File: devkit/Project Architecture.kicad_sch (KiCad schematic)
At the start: 0 parts

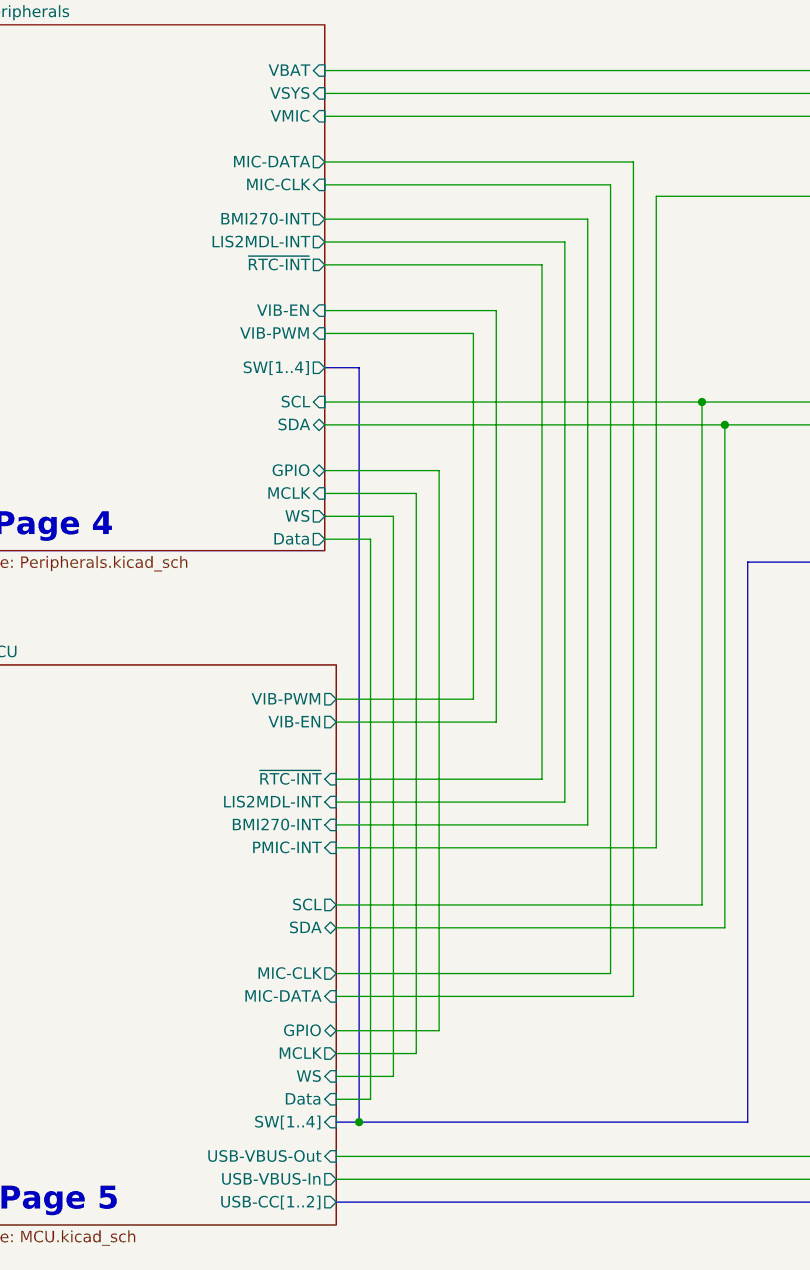
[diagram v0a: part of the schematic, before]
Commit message: Revert "Feature: Issue #180"
This reverts commit 364f4bbc8b17cbfb7f0155205af3315526997ba0.
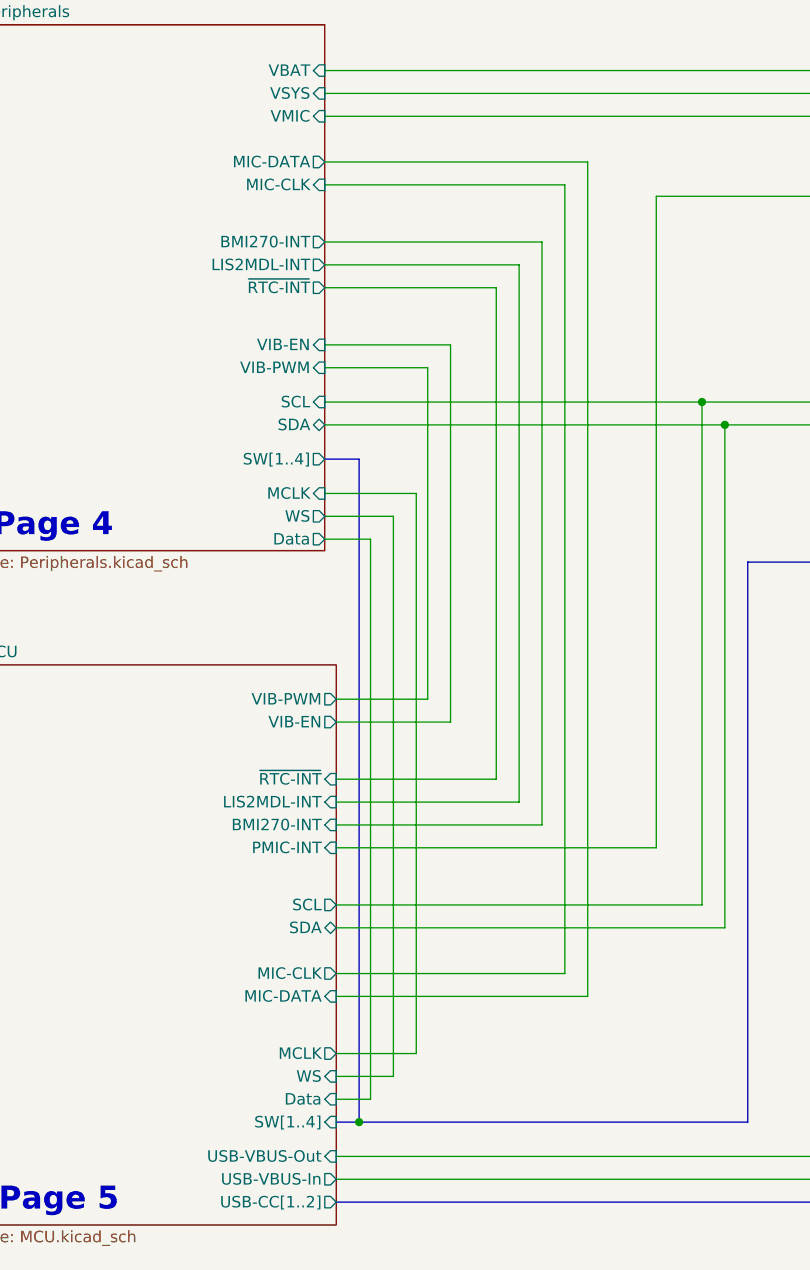
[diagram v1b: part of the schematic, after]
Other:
- sheet MCU ports: added none; removed GPIO
- sheet Peripherals ports: added none; removed GPIO
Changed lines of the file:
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@@
 	(wire
 		(pts
-			(xy 135.89 43.18) (xy 135.89 105.41)
-		)
-		(stroke
-			(width 0)
-			(type default)
-		)
-	)
-	(wire
-		(pts
-			(xy 140.97 36.83) (xy 109.22 36.83)
+			(xy 130.81 45.72) (xy 130.81 105.41)
+		)
+		(stroke
+			(width 0)
+			(type default)
+		)
+	)
+	(wire
+		(pts
+			(xy 135.89 36.83) (xy 109.22 36.83)
 		)
 		(stroke
@@
 	(wire
 		(pts
-			(xy 110.49 107.95) (xy 138.43 107.95)
+			(xy 110.49 107.95) (xy 133.35 107.95)
 		)
 		(stroke
@@
 	(wire
 		(pts
-			(xy 121.92 130.81) (xy 110.49 130.81)
-		)
-		(stroke
-			(width 0)
-			(type default)
-		)
-	)
-	(wire
-		(pts
-			(xy 133.35 102.87) (xy 110.49 102.87)
-		)
-		(stroke
-			(width 0)
-			(type default)
-		)
-	)
-	(wire
-		(pts
-			(xy 125.73 93.98) (xy 110.49 93.98)
+			(xy 128.27 102.87) (xy 110.49 102.87)
+		)
+		(stroke
+			(width 0)
+			(type default)
+		)
+	)
+	(wire
+		(pts
+			(xy 120.65 93.98) (xy 110.49 93.98)
 		)
 		(stroke
@@
 	(bus
 		(pts
-			(xy 113.03 57.15) (xy 113.03 140.97)
+			(xy 113.03 67.31) (xy 113.03 140.97)
 		)
 		(stroke
@@
 	(wire
 		(pts
-			(xy 138.43 107.95) (xy 138.43 40.64)
+			(xy 133.35 107.95) (xy 133.35 43.18)
 		)
 		(stroke
@@
 	(wire
 		(pts
-			(xy 135.89 105.41) (xy 110.49 105.41)
-		)
-		(stroke
-			(width 0)
-			(type default)
-		)
-	)
-	(wire
-		(pts
-			(xy 133.35 45.72) (xy 133.35 102.87)
+			(xy 130.81 105.41) (xy 110.49 105.41)
+		)
+		(stroke
+			(width 0)
+			(type default)
+		)
+	)
+	(wire
+		(pts
+			(xy 128.27 48.26) (xy 128.27 102.87)
 		)
 		(stroke
@@
 	(wire
 		(pts
-			(xy 109.22 45.72) (xy 133.35 45.72)
+			(xy 109.22 48.26) (xy 128.27 48.26)
 		)
 		(stroke
@@
 	(bus
 		(pts
-			(xy 109.22 57.15) (xy 113.03 57.15)
-		)
-		(stroke
-			(width 0)
-			(type default)
-		)
-	)
-	(wire
-		(pts
-			(xy 128.27 96.52) (xy 110.49 96.52)
+			(xy 109.22 67.31) (xy 113.03 67.31)
+		)
+		(stroke
+			(width 0)
+			(type default)
+		)
+	)
+	(wire
+		(pts
+			(xy 123.19 96.52) (xy 110.49 96.52)
 		)
 		(stroke
@@
 	(wire
 		(pts
-			(xy 109.22 53.34) (xy 125.73 53.34)
-		)
-		(stroke
-			(width 0)
-			(type default)
-		)
-	)
-	(wire
-		(pts
-			(xy 143.51 127) (xy 110.49 127)
+			(xy 109.22 57.15) (xy 120.65 57.15)
+		)
+		(stroke
+			(width 0)
+			(type default)
+		)
+	)
+	(wire
+		(pts
+			(xy 138.43 127) (xy 110.49 127)
 		)
 		(stroke
@@
 	(wire
 		(pts
-			(xy 138.43 40.64) (xy 109.22 40.64)
+			(xy 133.35 43.18) (xy 109.22 43.18)
 		)
 		(stroke
@@
 	(wire
 		(pts
-			(xy 140.97 124.46) (xy 140.97 36.83)
-		)
-		(stroke
-			(width 0)
-			(type default)
-		)
-	)
-	(wire
-		(pts
-			(xy 109.22 50.8) (xy 128.27 50.8)
+			(xy 135.89 124.46) (xy 135.89 36.83)
+		)
+		(stroke
+			(width 0)
+			(type default)
+		)
+	)
+	(wire
+		(pts
+			(xy 109.22 54.61) (xy 123.19 54.61)
 		)
 		(stroke
@@
 	(wire
 		(pts
-			(xy 110.49 124.46) (xy 140.97 124.46)
+			(xy 110.49 124.46) (xy 135.89 124.46)
 		)
 		(stroke
@@
 	(wire
 		(pts
-			(xy 121.92 68.58) (xy 121.92 130.81)
-		)
-		(stroke
-			(width 0)
-			(type default)
-		)
-	)
-	(wire
-		(pts
-			(xy 109.22 43.18) (xy 135.89 43.18)
+			(xy 109.22 45.72) (xy 130.81 45.72)
 		)
 		(stroke
@@
 	(wire
 		(pts
-			(xy 128.27 50.8) (xy 128.27 96.52)
+			(xy 123.19 54.61) (xy 123.19 96.52)
 		)
 		(stroke
@@
 	(wire
 		(pts
-			(xy 143.51 34.29) (xy 143.51 127)
-		)
-		(stroke
-			(width 0)
-			(type default)
-		)
-	)
-	(wire
-		(pts
-			(xy 125.73 53.34) (xy 125.73 93.98)
-		)
-		(stroke
-			(width 0)
-			(type default)
-		)
-	)
-	(wire
-		(pts
-			(xy 109.22 68.58) (xy 121.92 68.58)
+			(xy 138.43 34.29) (xy 138.43 127)
+		)
+		(stroke
+			(width 0)
+			(type default)
+		)
+	)
+	(wire
+		(pts
+			(xy 120.65 57.15) (xy 120.65 93.98)
 		)
 		(stroke
@@
 	(wire
 		(pts
-			(xy 109.22 34.29) (xy 143.51 34.29)
+			(xy 109.22 34.29) (xy 138.43 34.29)
 		)
 		(stroke
@@
 		)
 		(pin "LIS2MDL-INT" output
+			(at 109.22 45.72 0)
+			(effects
+				(font
+					(size 1.27 1.27)
+				)
+				(justify right)
+			)
+		)
+		(pin "BMI270-INT" output
 			(at 109.22 43.18 0)
-			(effects
-				(font
-					(size 1.27 1.27)
-				)
-				(justify right)
-			)
-		)
-		(pin "BMI270-INT" output
-			(at 109.22 40.64 0)
 			(effects
 				(font
@@
 		)
 		(pin "SW[1..4]" output
-			(at 109.22 57.15 0)
+			(at 109.22 67.31 0)
 			(effects
 				(font
@@
 		)
 		(pin "~{RTC-INT}" output
-			(at 109.22 45.72 0)
+			(at 109.22 48.26 0)
 			(effects
 				(font
@@
 		)
 		(pin "VIB-EN" input
-			(at 109.22 50.8 0)
+			(at 109.22 54.61 0)
 			(effects
 				(font
@@
 		)
 		(pin "VIB-PWM" input
-			(at 109.22 53.34 0)
+			(at 109.22 57.15 0)
 			(effects
 				(font
@@
 		(pin "VMIC" input
 			(at 109.22 29.21 0)
-			(effects
-				(font
-					(size 1.27 1.27)
-				)
-				(justify right)
-			)
-		)
-		(pin "GPIO" bidirectional
-			(at 109.22 68.58 0)
 			(effects
 				(font
@@
 			(effects
 				(font
-					(size 1.27 1.27)
-				)
-				(justify right)
-			)
-		)
-		(pin "GPIO" bidirectional
-			(at 110.49 130.81 0)
-			(effects
-				(font

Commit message: Feature: Issue #180
- Add additional pin to I2S header

Closes #180

Signed-off-by: Daniel Kampert <DanielKampert@kampis-elektroecke.de>
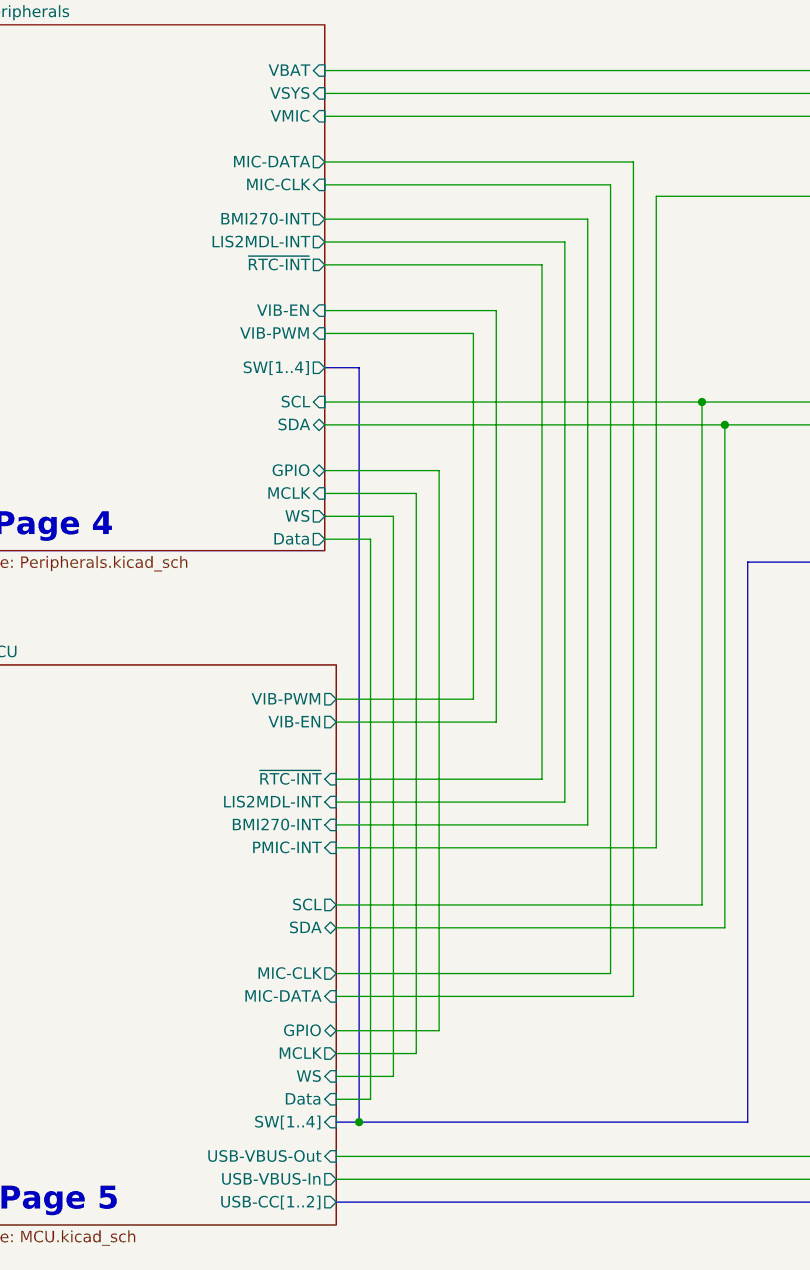
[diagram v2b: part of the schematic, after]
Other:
- sheet MCU ports: added GPIO; removed none
- sheet Peripherals ports: added GPIO; removed none
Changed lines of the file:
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@@
 	(wire
 		(pts
-			(xy 130.81 45.72) (xy 130.81 105.41)
-		)
-		(stroke
-			(width 0)
-			(type default)
-		)
-	)
-	(wire
-		(pts
-			(xy 135.89 36.83) (xy 109.22 36.83)
+			(xy 135.89 43.18) (xy 135.89 105.41)
+		)
+		(stroke
+			(width 0)
+			(type default)
+		)
+	)
+	(wire
+		(pts
+			(xy 140.97 36.83) (xy 109.22 36.83)
 		)
 		(stroke
@@
 	(wire
 		(pts
-			(xy 110.49 107.95) (xy 133.35 107.95)
+			(xy 110.49 107.95) (xy 138.43 107.95)
 		)
 		(stroke
@@
 	(wire
 		(pts
-			(xy 128.27 102.87) (xy 110.49 102.87)
-		)
-		(stroke
-			(width 0)
-			(type default)
-		)
-	)
-	(wire
-		(pts
-			(xy 120.65 93.98) (xy 110.49 93.98)
+			(xy 121.92 130.81) (xy 110.49 130.81)
+		)
+		(stroke
+			(width 0)
+			(type default)
+		)
+	)
+	(wire
+		(pts
+			(xy 133.35 102.87) (xy 110.49 102.87)
+		)
+		(stroke
+			(width 0)
+			(type default)
+		)
+	)
+	(wire
+		(pts
+			(xy 125.73 93.98) (xy 110.49 93.98)
 		)
 		(stroke
@@
 	(bus
 		(pts
-			(xy 113.03 67.31) (xy 113.03 140.97)
+			(xy 113.03 57.15) (xy 113.03 140.97)
 		)
 		(stroke
@@
 	(wire
 		(pts
-			(xy 133.35 107.95) (xy 133.35 43.18)
+			(xy 138.43 107.95) (xy 138.43 40.64)
 		)
 		(stroke
@@
 	(wire
 		(pts
-			(xy 130.81 105.41) (xy 110.49 105.41)
-		)
-		(stroke
-			(width 0)
-			(type default)
-		)
-	)
-	(wire
-		(pts
-			(xy 128.27 48.26) (xy 128.27 102.87)
+			(xy 135.89 105.41) (xy 110.49 105.41)
+		)
+		(stroke
+			(width 0)
+			(type default)
+		)
+	)
+	(wire
+		(pts
+			(xy 133.35 45.72) (xy 133.35 102.87)
 		)
 		(stroke
@@
 	(wire
 		(pts
-			(xy 109.22 48.26) (xy 128.27 48.26)
+			(xy 109.22 45.72) (xy 133.35 45.72)
 		)
 		(stroke
@@
 	(bus
 		(pts
-			(xy 109.22 67.31) (xy 113.03 67.31)
-		)
-		(stroke
-			(width 0)
-			(type default)
-		)
-	)
-	(wire
-		(pts
-			(xy 123.19 96.52) (xy 110.49 96.52)
+			(xy 109.22 57.15) (xy 113.03 57.15)
+		)
+		(stroke
+			(width 0)
+			(type default)
+		)
+	)
+	(wire
+		(pts
+			(xy 128.27 96.52) (xy 110.49 96.52)
 		)
 		(stroke
@@
 	(wire
 		(pts
-			(xy 109.22 57.15) (xy 120.65 57.15)
-		)
-		(stroke
-			(width 0)
-			(type default)
-		)
-	)
-	(wire
-		(pts
-			(xy 138.43 127) (xy 110.49 127)
+			(xy 109.22 53.34) (xy 125.73 53.34)
+		)
+		(stroke
+			(width 0)
+			(type default)
+		)
+	)
+	(wire
+		(pts
+			(xy 143.51 127) (xy 110.49 127)
 		)
 		(stroke
@@
 	(wire
 		(pts
-			(xy 133.35 43.18) (xy 109.22 43.18)
+			(xy 138.43 40.64) (xy 109.22 40.64)
 		)
 		(stroke
@@
 	(wire
 		(pts
-			(xy 135.89 124.46) (xy 135.89 36.83)
-		)
-		(stroke
-			(width 0)
-			(type default)
-		)
-	)
-	(wire
-		(pts
-			(xy 109.22 54.61) (xy 123.19 54.61)
+			(xy 140.97 124.46) (xy 140.97 36.83)
+		)
+		(stroke
+			(width 0)
+			(type default)
+		)
+	)
+	(wire
+		(pts
+			(xy 109.22 50.8) (xy 128.27 50.8)
 		)
 		(stroke
@@
 	(wire
 		(pts
-			(xy 110.49 124.46) (xy 135.89 124.46)
+			(xy 110.49 124.46) (xy 140.97 124.46)
 		)
 		(stroke
@@
 	(wire
 		(pts
-			(xy 109.22 45.72) (xy 130.81 45.72)
+			(xy 121.92 68.58) (xy 121.92 130.81)
+		)
+		(stroke
+			(width 0)
+			(type default)
+		)
+	)
+	(wire
+		(pts
+			(xy 109.22 43.18) (xy 135.89 43.18)
 		)
 		(stroke
@@
 	(wire
 		(pts
-			(xy 123.19 54.61) (xy 123.19 96.52)
+			(xy 128.27 50.8) (xy 128.27 96.52)
 		)
 		(stroke
@@
 	(wire
 		(pts
-			(xy 138.43 34.29) (xy 138.43 127)
-		)
-		(stroke
-			(width 0)
-			(type default)
-		)
-	)
-	(wire
-		(pts
-			(xy 120.65 57.15) (xy 120.65 93.98)
+			(xy 143.51 34.29) (xy 143.51 127)
+		)
+		(stroke
+			(width 0)
+			(type default)
+		)
+	)
+	(wire
+		(pts
+			(xy 125.73 53.34) (xy 125.73 93.98)
+		)
+		(stroke
+			(width 0)
+			(type default)
+		)
+	)
+	(wire
+		(pts
+			(xy 109.22 68.58) (xy 121.92 68.58)
 		)
 		(stroke
@@
 	(wire
 		(pts
-			(xy 109.22 34.29) (xy 138.43 34.29)
+			(xy 109.22 34.29) (xy 143.51 34.29)
 		)
 		(stroke
@@
 		)
 		(pin "LIS2MDL-INT" output
-			(at 109.22 45.72 0)
+			(at 109.22 43.18 0)
 			(effects
 				(font
@@
 		)
 		(pin "BMI270-INT" output
-			(at 109.22 43.18 0)
+			(at 109.22 40.64 0)
 			(effects
 				(font
@@
 		)
 		(pin "SW[1..4]" output
-			(at 109.22 67.31 0)
+			(at 109.22 57.15 0)
 			(effects
 				(font
@@
 		)
 		(pin "~{RTC-INT}" output
-			(at 109.22 48.26 0)
+			(at 109.22 45.72 0)
 			(effects
 				(font
@@
 		)
 		(pin "VIB-EN" input
-			(at 109.22 54.61 0)
+			(at 109.22 50.8 0)
 			(effects
 				(font
@@
 		)
 		(pin "VIB-PWM" input
-			(at 109.22 57.15 0)
+			(at 109.22 53.34 0)
 			(effects
 				(font
@@
 		(pin "VMIC" input
 			(at 109.22 29.21 0)
+			(effects
+				(font
+					(size 1.27 1.27)
+				)
+				(justify right)
+			)
+		)
+		(pin "GPIO" bidirectional
+			(at 109.22 68.58 0)
 			(effects
 				(font
@@
 			(effects
 				(font
+					(size 1.27 1.27)
+				)
+				(justify right)
+			)
+		)
+		(pin "GPIO" bidirectional
+			(at 110.49 130.81 0)
+			(effects
+				(font

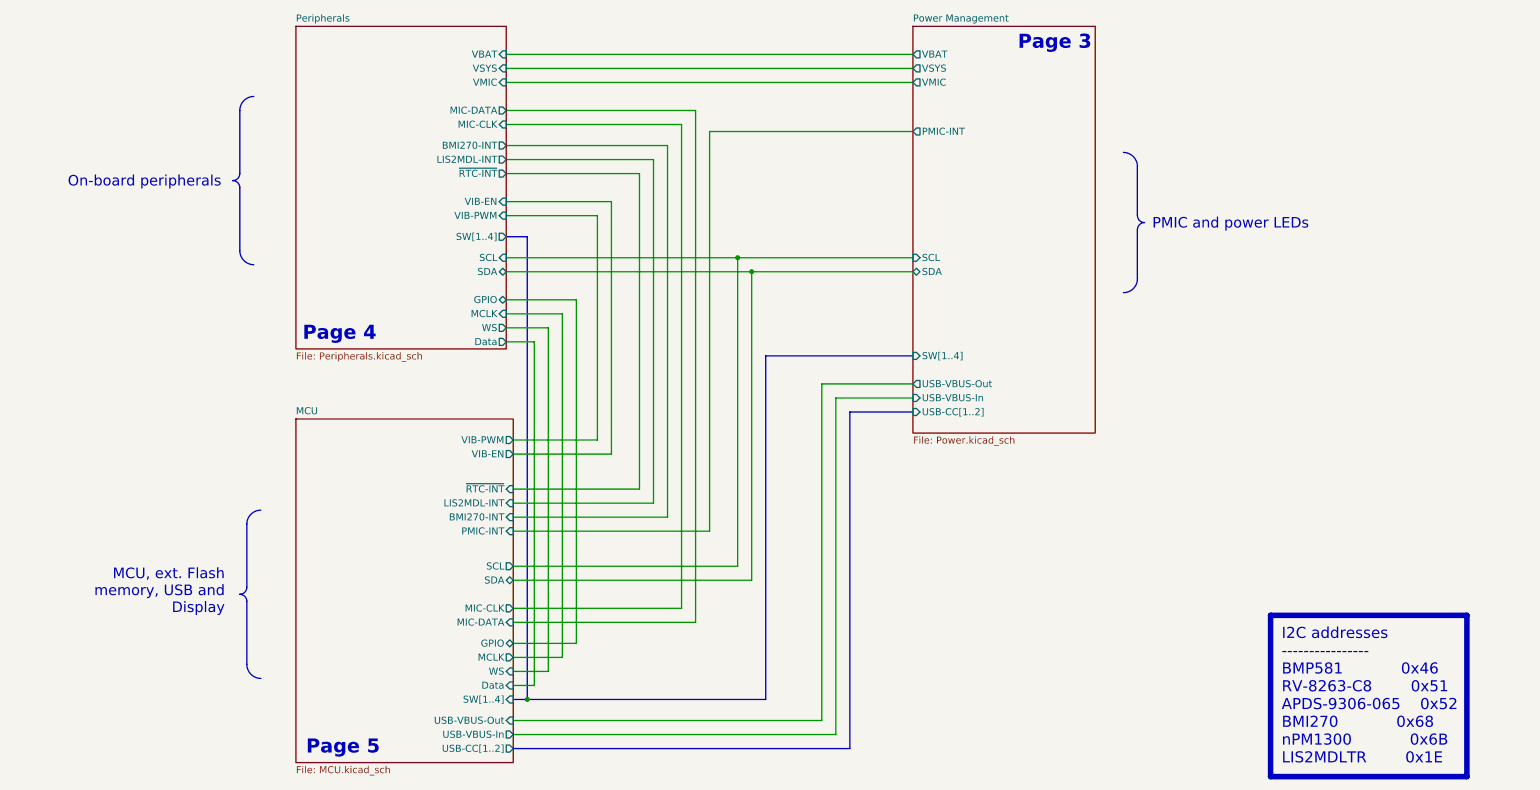
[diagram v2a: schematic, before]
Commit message: Fix wrong page numbers in Project Architecture schematic
Signed-off-by: Daniel Kampert <DanielKampert@kampis-elektroecke.de>
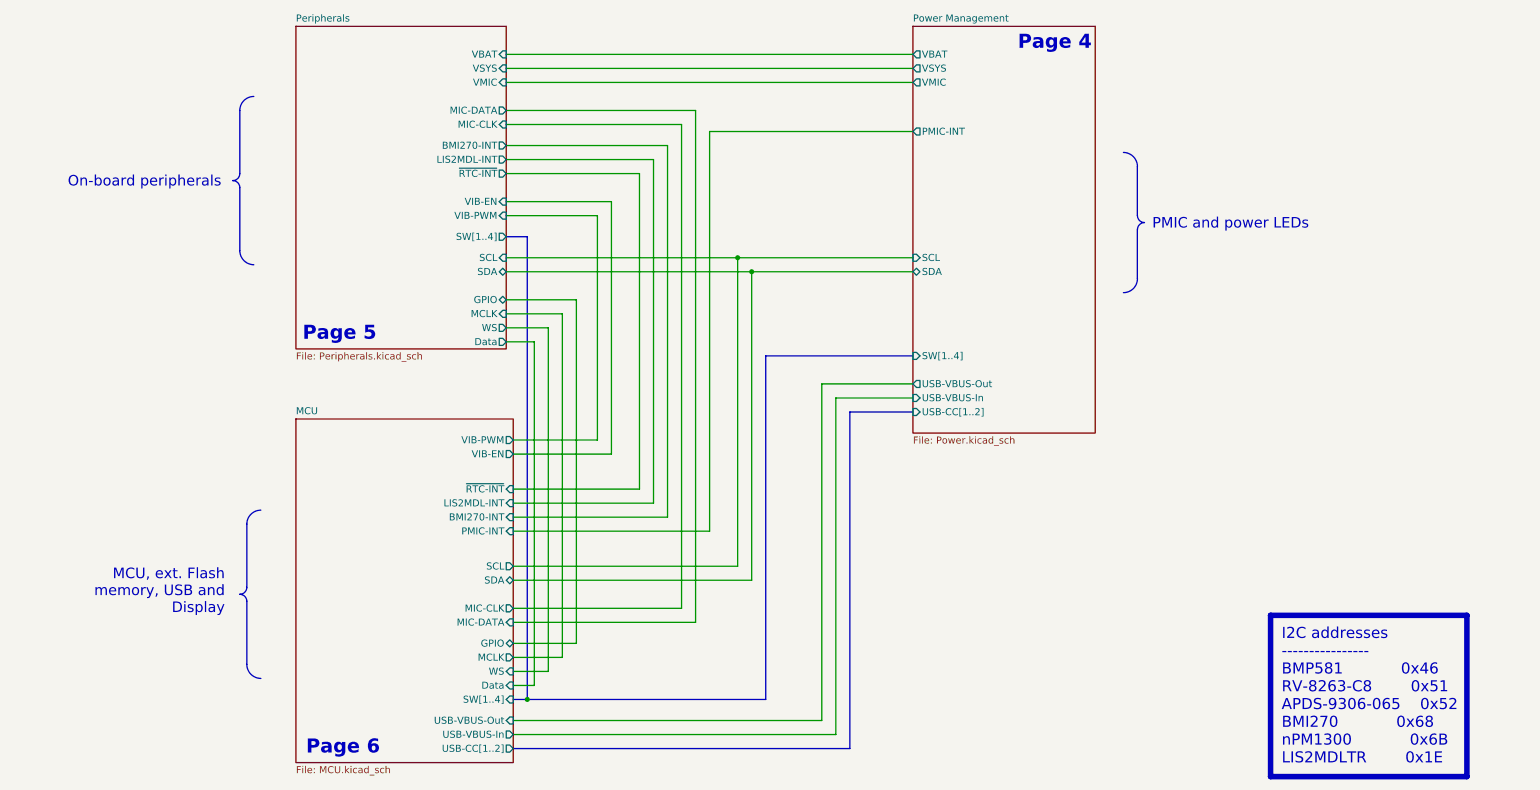
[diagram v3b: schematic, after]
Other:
- note added: "Page 6"
- note removed: "Page 3"
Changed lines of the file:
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@@
+		)
+	)
+	(text "Page 6"
+		(exclude_from_sim no)
+		(at 86.36 151.13 0)
+		(effects
+			(font
+				(size 2.54 2.54)
+				(bold yes)
+				(color 20 60 40 1)
+			)
+			(justify right bottom)
+			(href "#6")
+		)
+	)
+	(text "Page 4"
+		(exclude_from_sim no)
+		(at 215.265 23.495 0)
+		(effects
+			(font
+				(size 2.54 2.54)
+				(bold yes)
+				(color 20 60 40 1)
+			)
+			(justify right bottom)
+			(href "#4")
 		)
 	)
 	(text "Page 5"
 		(exclude_from_sim no)
-		(at 86.36 151.13 0)
+		(at 85.725 76.2 0)
 		(effects
 			(font
@@
 		)
 	)
-	(text "Page 3"
-		(exclude_from_sim no)
-		(at 215.265 23.495 0)
-		(effects
-			(font
-				(size 2.54 2.54)
-				(bold yes)
-				(color 20 60 40 1)
-			)
-			(justify right bottom)
-			(href "#3")
-		)
-	)
-	(text "Page 4"
-		(exclude_from_sim no)
-		(at 85.725 76.2 0)
-		(effects
-			(font
-				(size 2.54 2.54)
-				(bold yes)
-				(color 20 60 40 1)
-			)
-			(justify right bottom)
-			(href "#4")
-		)
-	)
